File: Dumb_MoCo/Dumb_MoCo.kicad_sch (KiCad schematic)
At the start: 17 parts, among them U1 VNH7070AS

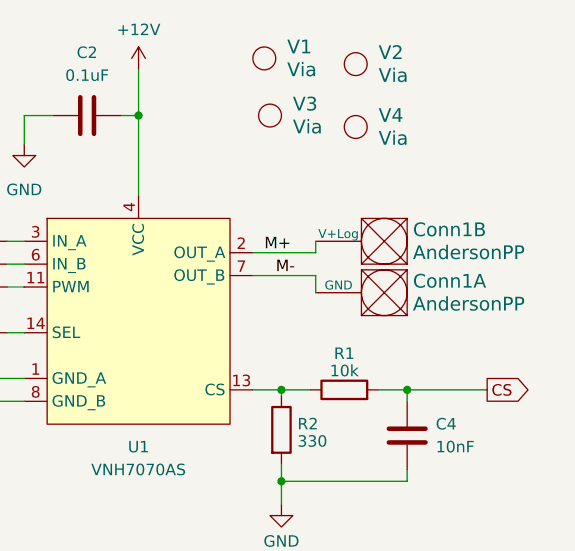
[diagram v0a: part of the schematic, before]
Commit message: Flipped VNH
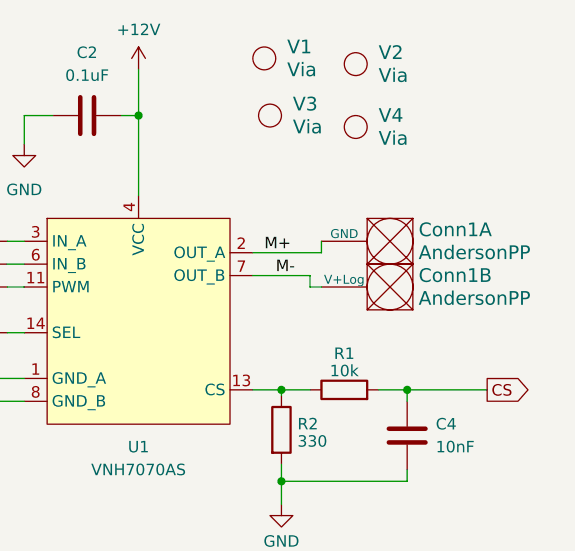
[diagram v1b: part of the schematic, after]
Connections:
- net M+: now also Conn1.1 (GND); no longer Conn1.2 (V+Log)
- net M-: now also Conn1.2 (V+Log); no longer Conn1.1 (GND)
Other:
- moved on the sheet: Conn1A, Conn1B
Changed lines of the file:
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@@
-	(wire
-		(pts
-			(xy 106.045 45.72) (xy 106.045 44.45)
-		)
-		(stroke
-			(width 0)
-			(type default)
-		)
-	)
 	(wire
 		(pts
@@
 	(wire
 		(pts
-			(xy 99.06 45.72) (xy 106.045 45.72)
+			(xy 99.06 45.72) (xy 106.68 45.72)
 		)
 		(stroke
@@
 	(wire
 		(pts
+			(xy 106.68 44.45) (xy 106.68 45.72)
+		)
+		(stroke
+			(width 0)
+			(type default)
+		)
+	)
+	(wire
+		(pts
 			(xy 40.005 31.75) (xy 40.005 33.655)
 		)
@@
 	(wire
 		(pts
-			(xy 106.045 48.26) (xy 106.045 50.165)
-		)
-		(stroke
-			(width 0)
-			(type default)
-		)
-	)
-	(wire
-		(pts
 			(xy 40.005 43.18) (xy 40.005 45.085)
 		)
@@
 	(wire
 		(pts
-			(xy 99.06 48.26) (xy 106.045 48.26)
+			(xy 105.41 49.53) (xy 106.68 49.53)
 		)
 		(stroke
@@
 		(pts
 			(xy 71.755 44.45) (xy 73.66 44.45)
+		)
+		(stroke
+			(width 0)
+			(type default)
+		)
+	)
+	(wire
+		(pts
+			(xy 105.41 48.26) (xy 99.06 48.26)
+		)
+		(stroke
+			(width 0)
+			(type default)
+		)
+	)
+	(wire
+		(pts
+			(xy 105.41 49.53) (xy 105.41 48.26)
 		)
 		(stroke
@@
 	(symbol
 		(lib_id "MRDT_Connectors:AndersonPP")
-		(at 116.205 41.91 180)
+		(at 116.84 46.99 180)
 		(unit 2)
 		(exclude_from_sim no)
@@
 		(fields_autoplaced yes)
 		(property "Reference" "Conn1"
-			(at 116.84 43.18 0)
+			(at 117.475 48.26 0)
 			(effects
 				(font
@@
 		)
 		(property "Value" "AndersonPP"
-			(at 116.84 45.72 0)
+			(at 117.475 50.8 0)
 			(effects
 				(font
@@
 		)
 		(property "Footprint" "MRDT_Connectors:Square_Anderson_2_H_Side_By_Side"
-			(at 120.015 27.94 0)
+			(at 120.65 33.02 0)
 			(effects
 				(font
@@
 		)
 		(property "Datasheet" ""
-			(at 120.015 27.94 0)
-			(effects
-				(font
-					(size 1.524 1.524)
-				)
-				(hide yes)
-			)
-		)
-		(property "Description" ""
-			(at 116.205 41.91 0)
+			(at 120.65 33.02 0)
+			(effects
+				(font
+					(size 1.524 1.524)
+				)
+				(hide yes)
+			)
+		)
+		(property "Description" ""
+			(at 116.84 46.99 0)
 			(effects
 				(font
@@
 	(symbol
 		(lib_id "MRDT_Connectors:AndersonPP")
-		(at 116.205 47.625 180)
+		(at 116.84 41.91 180)
 		(unit 1)
 		(exclude_from_sim no)
@@
 		(fields_autoplaced yes)
 		(property "Reference" "Conn1"
-			(at 116.84 48.895 0)
+			(at 117.475 43.18 0)
 			(effects
 				(font
@@
 		)
 		(property "Value" "AndersonPP"
-			(at 116.84 51.435 0)
+			(at 117.475 45.72 0)
 			(effects
 				(font
@@
 		)
 		(property "Footprint" "MRDT_Connectors:Square_Anderson_2_H_Side_By_Side"
-			(at 120.015 33.655 0)
+			(at 120.65 27.94 0)
 			(effects
 				(font
@@
 		)
 		(property "Datasheet" ""
-			(at 120.015 33.655 0)
-			(effects
-				(font
-					(size 1.524 1.524)
-				)
-				(hide yes)
-			)
-		)
-		(property "Description" ""
-			(at 116.205 47.625 0)
-			(effects
-				(font
+			(at 120.65 27.94 0)
+			(effects
+				(font
+					(size 1.524 1.524)
+				)
+				(hide yes)
+			)
+		)
+		(property "Description" ""
+			(at 116.84 41.91 0)
+			(effects
+				(font

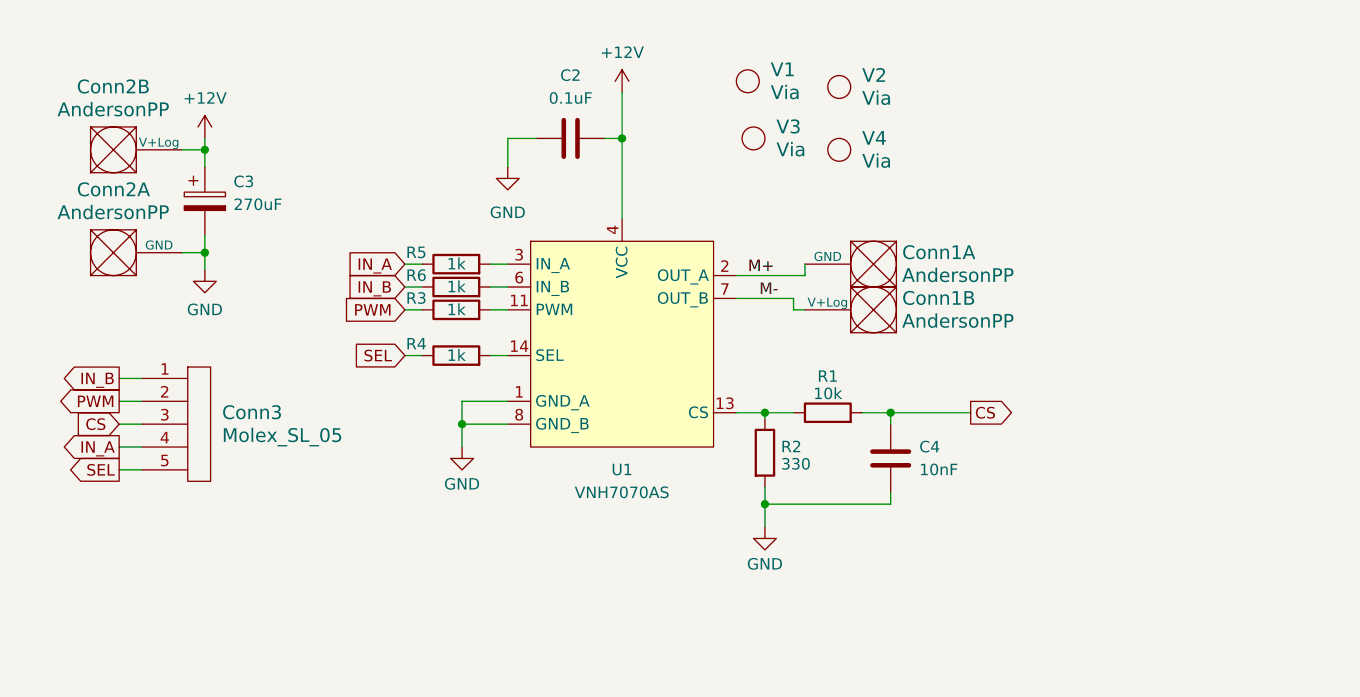
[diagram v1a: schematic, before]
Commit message: Swapped for new VNH IC
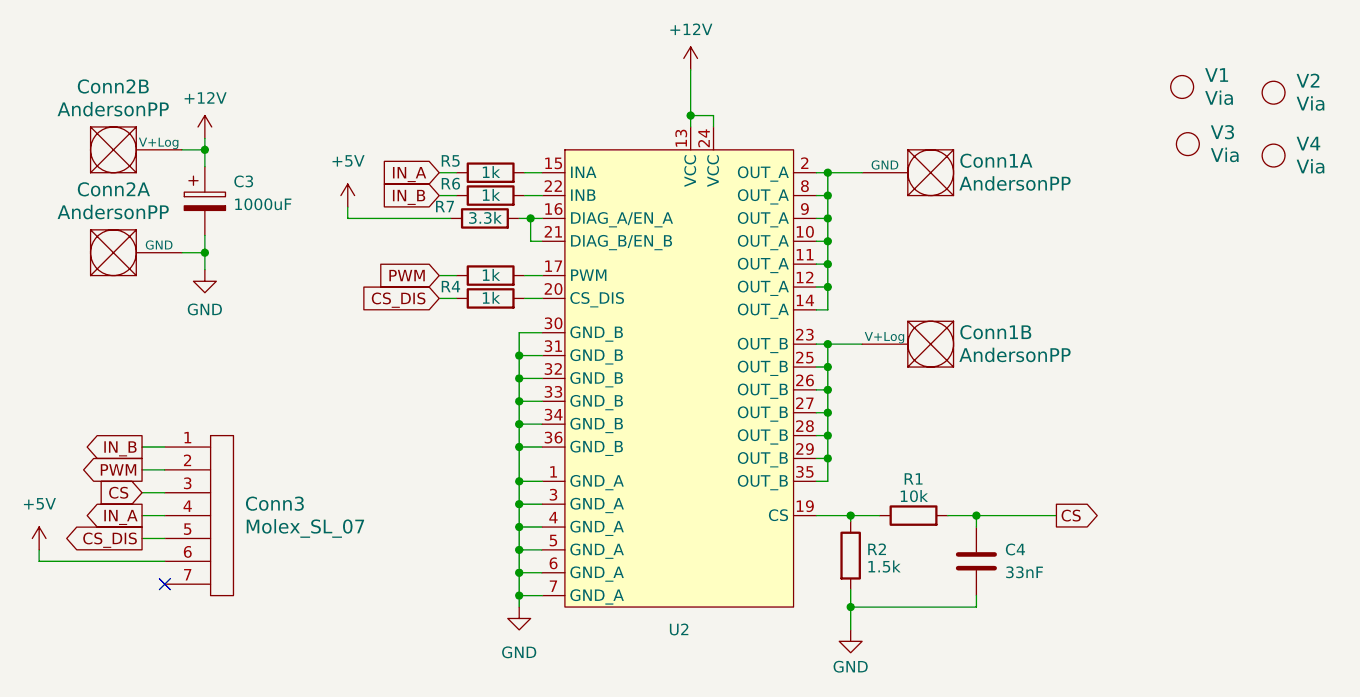
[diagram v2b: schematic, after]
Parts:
- removed C2: 0.1uF, Capacitor_SMD:C_0603_1608Metric_Pad1.08x0.95mm_HandSolder, symbol Device:C
- removed Conn3: Molex_SL_05, MRDT_Connectors:MOLEX_SL_05_Horizontal, symbol MRDT_Connectors:Molex_SL_05
- removed U1: VNH7070AS, Package_SO:SOIC-16_3.9x9.9mm_P1.27mm, symbol MRDT_Devices:VNH7070AS
- added Conn3: Molex_SL_07, MRDT_Connectors:MOLEX_SL_07_Horizontal, symbol MRDT_Connectors:Molex_SL_07
- added R7: 3.3k, Resistor_SMD:R_0603_1608Metric_Pad0.98x0.95mm_HandSolder, symbol Device:R
- added U2: ~, Package_SO:ST_PowerSSO-36_TP, symbol MRDT_Devices:VNH5050A-E
- C3: value 270uF -> 1000uF; footprint Capacitor_THT:CP_Radial_D8.0mm_P3.50mm -> Capacitor_THT:CP_Radial_D10.0mm_P5.00mm
- C4: value 10nF -> 33nF
- R2: value 330 -> 1.5k
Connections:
- net +12V: now also U2.13 (VCC), U2.24 (VCC)
- net CS: now also Conn3.3
- net GND: now also U2.1 (GND_A), U2.3 (GND_A), U2.30 (GND_B), U2.31 (GND_B), U2.32 (GND_B), U2.33 (GND_B), U2.34 (GND_B), U2.36 (GND_B), U2.4 (GND_A), U2.5 (GND_A), U2.6 (GND_A), U2.7 (GND_A)
- net IN_A: now also Conn3.4
- net IN_B: now also Conn3.1
- net PWM: now also Conn3.2
- net at R4.2: now also U2.20 (CS_DIS)
- net at R1.1, R2.1: now also U2.19 (CS)
- net at R5.2: now also U2.15 (INA)
- net at R3.2: now also U2.17 (PWM)
- net at R6.2: now also U2.22 (INB)
- net M+: no longer names the net of Conn1.1 (GND)
- net M+: now also U2.10 (OUT_A), U2.11 (OUT_A), U2.12 (OUT_A), U2.14 (OUT_A), U2.2 (OUT_A), U2.8 (OUT_A), U2.9 (OUT_A)
- net M-: no longer names the net of Conn1.2 (V+Log)
- net M-: now also U2.23 (OUT_B), U2.25 (OUT_B), U2.26 (OUT_B), U2.27 (OUT_B), U2.28 (OUT_B), U2.29 (OUT_B), U2.35 (OUT_B)
- net SEL renamed CS_DIS
- net CS_DIS: now also Conn3.5
- new net: R7.2, U2.16 (DIAG_A/EN_A), U2.21 (DIAG_B/EN_B)
- new net +5V: Conn3.6, R7.1
- no-connect marks 0 -> 1
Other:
- moved on the sheet: C4, Conn1A, Conn1B, R1, R2, R4, R5, R6, V1, V2, V3, V4
